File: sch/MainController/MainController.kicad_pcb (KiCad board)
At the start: 2 copper layers, 100.8 x 72.3 mm, 19 parts, among them J1 Power Input, J2 Sensor_CH1, J3 Sensor_CH2, J4 Sensor_CH3, J5 DIP_SW_IN, J6 Screw_Terminal_01x02, Q1 IRFZ44N, U1 SZH-PWSD-016

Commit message: [PCB] housekeeping
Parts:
- D2: value FR107 -> 1N5822
- J2, J3, J4: footprint TerminalBlock_Dinkle2:ECH381V-3p -> TerminalBlock_Dinkle2:ECH381R-3p
- moved D2 0.13 mm to (174.4, 102.4)

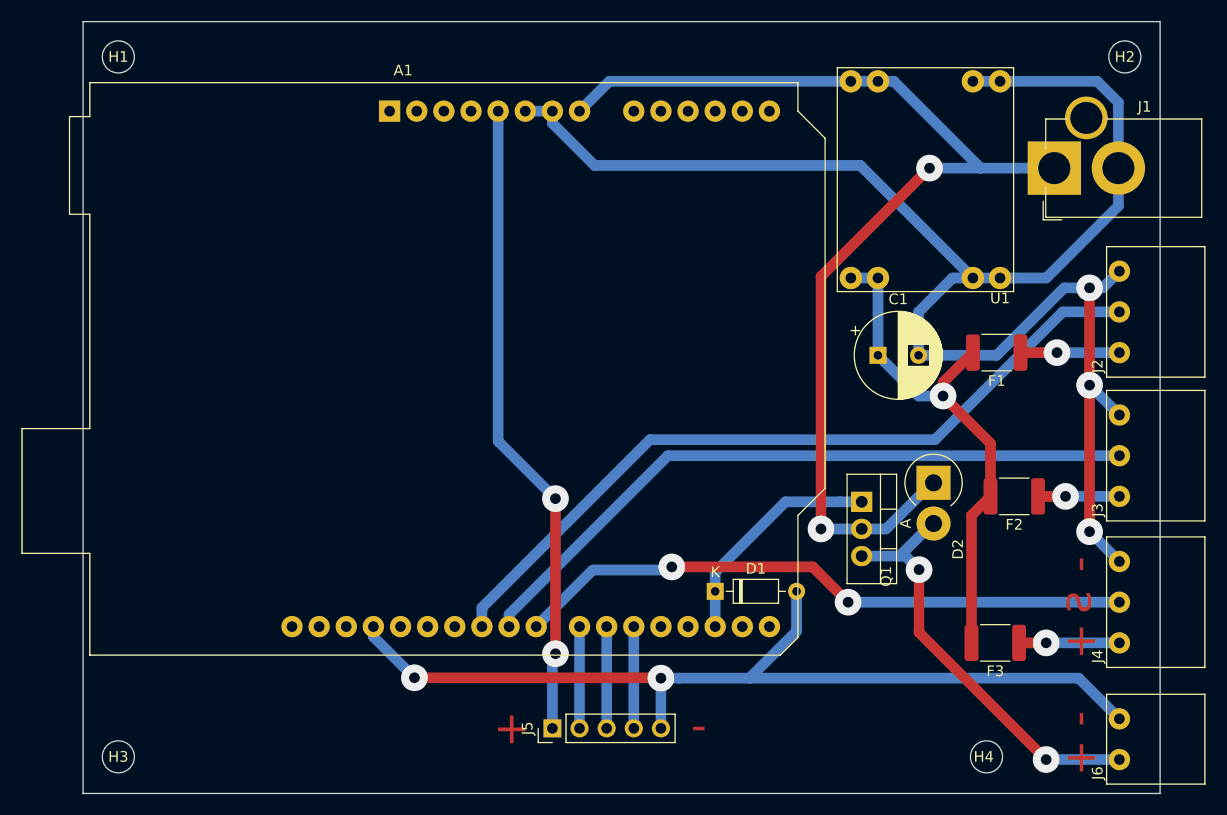
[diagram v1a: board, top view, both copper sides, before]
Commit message: [pcb] update pcb pattern
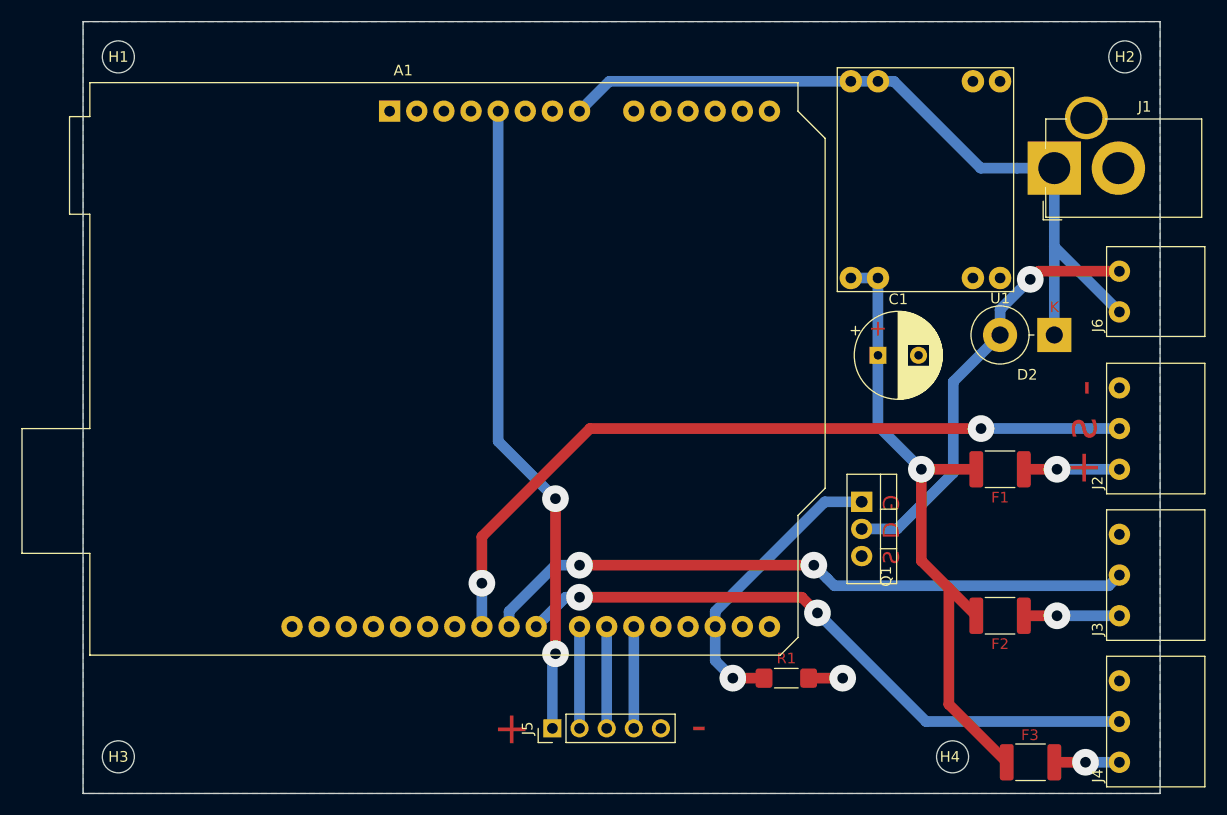
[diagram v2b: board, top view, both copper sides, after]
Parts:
- removed D1: 1N4148, Diode_THT:D_DO-35_SOD27_P7.62mm_Horizontal
- added R1: 10K, Resistor_SMD:R_1806_4516Metric_Pad1.57x1.80mm_HandSolder, F.Cu at (160.6, 120.7)
- D2: footprint Diode_THT:D_DO-201AD_P3.81mm_Vertical_AnodeUp -> Diode_THT:D_DO-201AD_P5.08mm_Vertical_KathodeUp
- moved J6 41.9 mm to (191.8, 86.4)
- moved D2 17.9 mm to (185.7, 88.5), turned to 180 degrees
- moved F3 11.7 mm to (183.4, 128.5)
- moved F2 11.3 mm to (180.6, 114.8)
- moved J3 11.2 mm to (191.8, 114.8)
- moved J4 11.2 mm to (191.8, 128.5)
- moved F1 10.9 mm to (180.6, 101.1)
- moved J2 10.9 mm to (191.8, 101.1)
- moved H4 3.18 mm to (176.1, 128.0)
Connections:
- J6 pad 1: Net-(D2-Pad2) -> /12V_input
- J6 pad 2: GND -> Net-(D2-Pad2)
- Q1 pad 2: /12V_input -> Net-(D2-Pad2)
- Q1 pad 3: Net-(D2-Pad2) -> GND
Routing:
- net GND: track 241.6 -> 3.21 mm, vias 5 -> 1
- net /12V_input: track 104.3 -> 73.8 mm, vias 2 -> 0
- net /5V_ext: track 48.4 -> 61.7 mm
- net /SIG_OUT: track 22.1 -> 28.3 mm, vias 0 -> 1
- net Net-(F3-Pad1): track 9.40 -> 6.10 mm
- net /SIG_2: track 64.4 -> 61.6 mm, vias 0 -> 2
- net /SIG_3: track 58.3 -> 60.6 mm
- net Net-(D2-Pad2): track 39.8 -> 41.5 mm, vias 2 -> 1
- net Net-(F2-Pad1): track 7.62 -> 8.95 mm
- net /SIG_1: track 72.9 -> 72.3 mm, vias 0 -> 2
- added copper zone on B.Cu, net GND
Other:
- rule pad_to_mask_clearance: 0.051 -> 0.1
- board text added: "D"
- board text added: "G"
- board text added: "S"

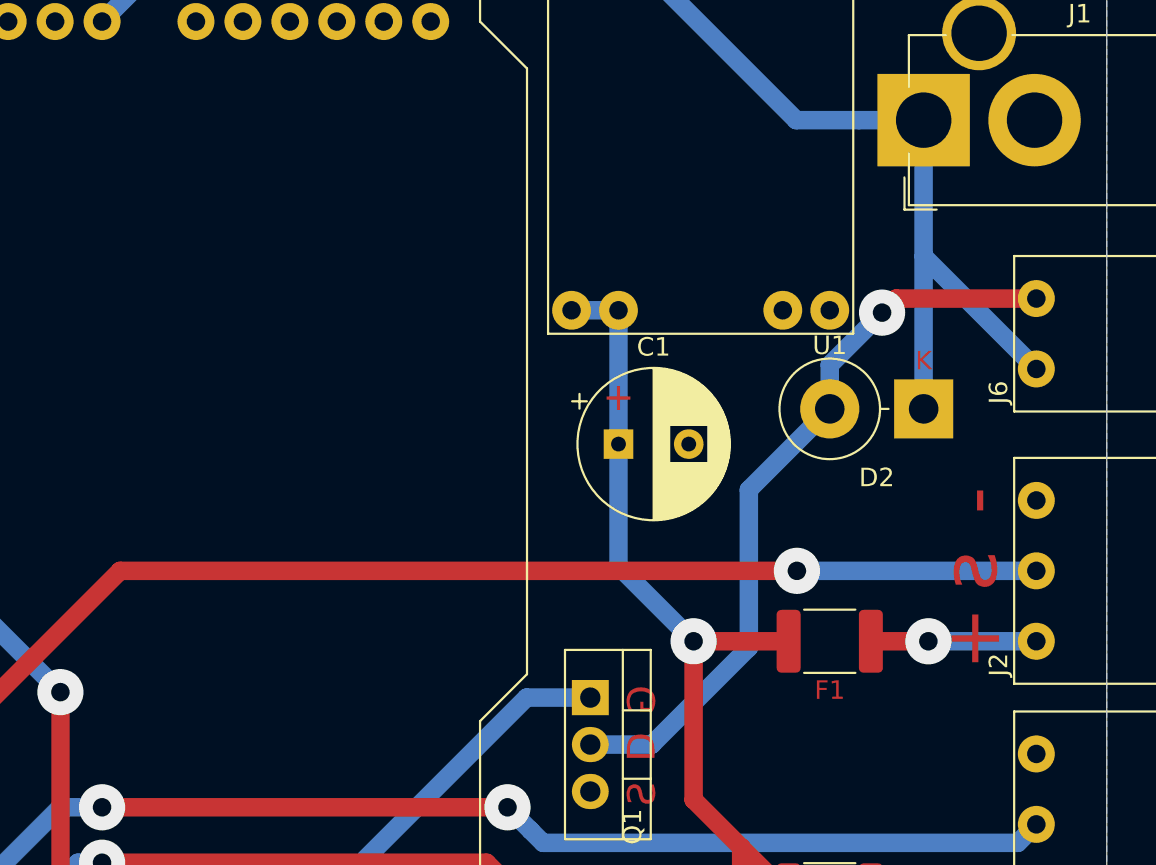
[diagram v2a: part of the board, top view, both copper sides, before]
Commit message: [pcb] fix tr control circuit and update pcb layout
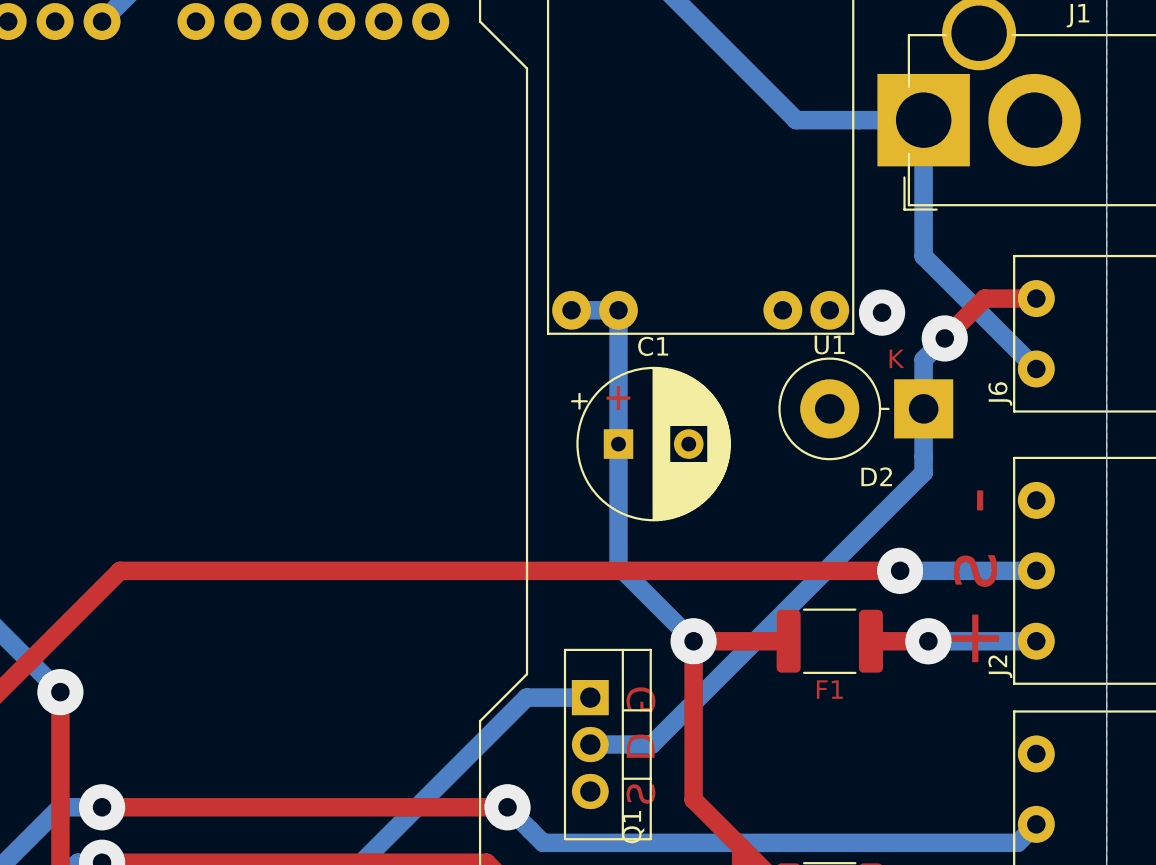
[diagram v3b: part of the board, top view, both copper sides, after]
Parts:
- C1: value CP -> 330uF
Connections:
- D2 pad 1: /12V_input -> Net-(D2-Pad1)
- D2 pad 2: Net-(D2-Pad2) -> GND
- J6 pad 2: Net-(D2-Pad2) -> Net-(D2-Pad1)
- Q1 pad 2: Net-(D2-Pad2) -> Net-(D2-Pad1)
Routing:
- net Net-(D2-Pad2): track 41.5 -> 0.00 mm
- net Net-(D2-Pad1): track 0.00 -> 37.7 mm, vias 0 -> 1
- net /12V_input: track 73.8 -> 65.5 mm
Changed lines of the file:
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@@
     (zones 0)
     (modules 19)
-    (nets 16)
+    (nets 17)
   )
   (page A4)
@@
   (net 14 /SIG_OUT)
   (net 15 "Net-(D2-Pad2)")
+  (net 16 "Net-(D2-Pad1)")
   (net_class Default "This is the default net class."
     (clearance 0.5)
@@
     (add_net /SW_3)
     (add_net GND)
+    (add_net "Net-(D2-Pad1)")
     (add_net "Net-(D2-Pad2)")
     (add_net "Net-(F1-Pad1)")
@@
       (net 14 /SIG_OUT))
     (pad 2 thru_hole oval (at 2.54 0 270) (size 1.905 2) (drill 1.1) (layers *.Cu *.Mask)
-      (net 15 "Net-(D2-Pad2)"))
+      (net 16 "Net-(D2-Pad1)"))
     (pad 3 thru_hole oval (at 5.08 0 270) (size 1.905 2) (drill 1.1) (layers *.Cu *.Mask)
       (net 5 GND))
@@
       (effects (font (size 1 1) (thickness 0.15)))
     )
-    (fp_text value CP (at 1.905 5.08) (layer F.Fab)
+    (fp_text value 330uF (at 1.905 5.08) (layer F.Fab)
       (effects (font (size 1 1) (thickness 0.15)))
     )
@@
       (net 8 /12V_input))
     (pad 2 thru_hole circle (at 3.81 0 90) (size 2 2) (drill 1) (layers *.Cu *.Mask)
-      (net 15 "Net-(D2-Pad2)"))
+      (net 16 "Net-(D2-Pad1)"))
     (model ${USER_LIB_DIR}/TerminalBlock_Dinkle2/packages3d/ECH381R-2p.STEP
       (offset (xyz 2 -8 3.5))
@@
       (effects (font (size 1 1) (thickness 0.15)))
     )
-    (fp_text user K (at 0 2.6) (layer F.Fab)
-      (effects (font (size 1 1) (thickness 0.15)))
-    )
-    (fp_text user K (at 0 2.6) (layer F.Cu)
+    (fp_text user K (at 1.524 2.6) (layer F.Fab)
+      (effects (font (size 1 1) (thickness 0.15)))
+    )
+    (fp_text user K (at 1.524 2.667) (layer F.Cu)
       (effects (font (size 1 1) (thickness 0.15)))
     )
     (pad 1 thru_hole rect (at 0 0 180) (size 3.2 3.2) (drill 1.6) (layers *.Cu *.Mask)
-      (net 8 /12V_input))
+      (net 16 "Net-(D2-Pad1)"))
     (pad 2 thru_hole oval (at 5.08 0 180) (size 3.2 3.2) (drill 1.6) (layers *.Cu *.Mask)
-      (net 15 "Net-(D2-Pad2)"))
+      (net 5 GND))
     (model ${KISYS3DMOD}/Diode_THT.3dshapes/D_DO-201AD_P5.08mm_Vertical_KathodeUp.wrl
       (at (xyz 0 0 0))
@@
   (via (at 165.862 120.65) (size 2.5) (drill 1) (layers F.Cu B.Cu) (net 5))
   (segment (start 162.671 120.65) (end 165.862 120.65) (width 1) (layer F.Cu) (net 5) (status 10))
-  (via (at 178.816 97.282) (size 2.5) (drill 1) (layers F.Cu B.Cu) (net 6))
-  (segment (start 191.77 97.282) (end 178.816 97.282) (width 1) (layer B.Cu) (net 6) (status 10))
   (via (at 132.08 111.76) (size 2.5) (drill 1) (layers F.Cu B.Cu) (net 6))
   (segment (start 132.08 107.403832) (end 132.08 111.76) (width 1) (layer F.Cu) (net 6))
-  (segment (start 178.816 97.282) (end 142.201832 97.282) (width 1) (layer F.Cu) (net 6))
   (segment (start 142.201832 97.282) (end 132.08 107.403832) (width 1) (layer F.Cu) (net 6))
   (segment (start 132.08 115.82) (end 132.084 115.824) (width 1) (layer B.Cu) (net 6) (status 30))
   (segment (start 132.08 111.76) (end 132.08 115.82) (width 1) (layer B.Cu) (net 6) (status 20))
+  (via (at 184.404 97.282) (size 2.5) (drill 1) (layers F.Cu B.Cu) (net 6))
+  (segment (start 142.201832 97.282) (end 184.404 97.282) (width 1) (layer F.Cu) (net 6))
+  (segment (start 184.404 97.282) (end 191.77 97.282) (width 1) (layer B.Cu) (net 6))
   (via (at 141.224 110.073994) (size 2.5) (drill 1) (layers F.Cu B.Cu) (net 7))
   (segment (start 163.159994 110.073994) (end 141.224 110.073994) (width 1) (layer F.Cu) (net 7))
@@
   (segment (start 169.164 64.77) (end 170.648924 64.77) (width 1) (layer B.Cu) (net 8) (status 10))
   (segment (start 185.293 73.279) (end 185.674 72.898) (width 1) (layer B.Cu) (net 8) (status 30))
-  (segment (start 191.77 86.36) (end 185.674 80.264) (width 1) (layer B.Cu) (net 8) (status 10))
-  (segment (start 185.674 72.898) (end 185.674 88.519) (width 1) (layer B.Cu) (net 8) (status 30))
+  (segment (start 185.674 80.264) (end 191.77 86.36) (width 1) (layer B.Cu) (net 8))
+  (segment (start 185.674 72.898) (end 185.674 80.264) (width 1) (layer B.Cu) (net 8))
   (via (at 163.497991 114.54399) (size 2.5) (drill 1) (layers F.Cu B.Cu) (net 9))
   (segment (start 191.77 124.714) (end 173.668001 124.714) (width 1) (layer B.Cu) (net 9) (status 10))
@@
   (segment (start 153.924 118.999) (end 155.575 120.65) (width 1) (layer B.Cu) (net 14))
   (segment (start 155.575 120.65) (end 158.496 120.65) (width 1) (layer F.Cu) (net 14) (status 20))
-  (segment (start 176.215999 92.897001) (end 180.594 88.519) (width 1) (layer B.Cu) (net 15) (status 20))
-  (segment (start 167.64 106.68) (end 170.970002 106.68) (width 1) (layer B.Cu) (net 15) (status 10))
-  (segment (start 170.970002 106.68) (end 176.215999 101.434003) (width 1) (layer B.Cu) (net 15))
-  (segment (start 176.215999 101.434003) (end 176.215999 92.897001) (width 1) (layer B.Cu) (net 15))
-  (segment (start 180.594 88.519) (end 180.594 87.539) (width 1) (layer B.Cu) (net 15) (status 30))
-  (segment (start 180.594 88.519) (end 180.594 86.142) (width 1) (layer B.Cu) (net 15) (status 10))
   (via (at 183.424 83.312) (size 2.5) (drill 1) (layers F.Cu B.Cu) (net 15))
-  (segment (start 180.594 86.142) (end 183.424 83.312) (width 1) (layer B.Cu) (net 15))
-  (segment (start 184.186 82.55) (end 183.424 83.312) (width 1) (layer F.Cu) (net 15))
-  (segment (start 191.77 82.55) (end 184.186 82.55) (width 1) (layer F.Cu) (net 15) (status 10))
+  (segment (start 185.674 91.976002) (end 185.674 91.119) (width 1) (layer B.Cu) (net 16))
+  (segment (start 170.970002 106.68) (end 185.674 91.976002) (width 1) (layer B.Cu) (net 16))
+  (segment (start 185.674 91.119) (end 185.674 88.519) (width 1) (layer B.Cu) (net 16))
+  (segment (start 167.64 106.68) (end 170.970002 106.68) (width 1) (layer B.Cu) (net 16))
+  (segment (start 185.674 88.519) (end 185.674 85.852) (width 1) (layer B.Cu) (net 16))
+  (via (at 186.817 84.709) (size 2.5) (drill 1) (layers F.Cu B.Cu) (net 16))
+  (segment (start 185.674 85.852) (end 186.817 84.709) (width 1) (layer B.Cu) (net 16))
+  (segment (start 188.976 82.55) (end 186.817 84.709) (width 1) (layer F.Cu) (net 16))
+  (segment (start 191.77 82.55) (end 188.976 82.55) (width 1) (layer F.Cu) (net 16))
   (zone (net 5) (net_name GND) (layer B.Cu) (hatch edge 0.508)
     (connect_pads (clearance 1))
